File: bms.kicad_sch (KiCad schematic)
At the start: 0 parts

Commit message: Ajout du BMS
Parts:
- added C10, C13, C14, C15, C21, C8, C9: 100nF, Capacitor_SMD:C_0805_2012Metric, symbol local:C_0402
- added C11, C23, C24, C25: 1µF, Capacitor_SMD:C_0805_2012Metric, symbol local:C_0402
- added C12: 47nF, Capacitor_SMD:C_0805_2012Metric, symbol local:C_0402
- added C16: 20µF, Capacitor_SMD:C_0805_2012Metric, symbol local:C_0402
- added C17: 2.2µF, Capacitor_SMD:C_0805_2012Metric, symbol local:C_0402
- added C18, C19, C20: 220nF, Capacitor_SMD:C_0805_2012Metric, symbol local:C_0402
- added C22: 100pF, Capacitor_SMD:C_0805_2012Metric, symbol local:C_0402
- added C6: 42nF, Capacitor_SMD:C_0805_2012Metric, symbol local:C_0402
- added C7: 1nF, Capacitor_SMD:C_0805_2012Metric, symbol local:C_0402
- added IC3: BQ24810RUYR, local:QFN40P400X400X80-29N-D, symbol local:BQ24810RUYR
- added J2: S4B-XH-A-1, S4B-XH-A-1:JST_S4B-XH-A-1, symbol local:S4B-XH-A-1
- added L2: 3.3µH, symbol Device:L
- added R10, R17, R9: 4k, Resistor_SMD:R_0805_2012Metric, symbol local:R
- added R11: 866k, Resistor_SMD:R_0805_2012Metric, symbol local:R
- added R12: 133k, Resistor_SMD:R_0805_2012Metric, symbol local:R
- added R13: 0.01, Resistor_SMD:R_0805_2012Metric, symbol local:R
- added R14, R15, R16, R18, R19, R20, R22, R23: 10, Resistor_SMD:R_0805_2012Metric, symbol local:R
- added R21, R6: 0.001, Resistor_SMD:R_0805_2012Metric, symbol local:R
- added R24, R25: 5.1k, Resistor_SMD:R_0805_2012Metric, symbol local:R
- added R7, R8: 4.99, Resistor_SMD:R_0805_2012Metric, symbol local:R
- added U1, U2, U3, U4, U5, U7, U8: XSM6K519NW, local:DFN2020MD-6_SOT1220_NEX, symbol local:XSM6K519NW
- added U6: BQ76905RGRR, local:IC_BQ76905RGRR, symbol local:BQ76905RGRR
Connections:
- new net: C12.1, IC3.27 (PHASE), L2.1, U3.4, U3.7, U4.1, U4.2, U4.5, U4.6, U4.8
- new net: IC3.23 (LODRV), U4.3
- new net: C10.2, C8.2, IC3.1 (ACN), R8.2
- new net: IC3.17 (BATSRC), R16.1
- new net: IC3.18 (BATDRV), R17.1
- new net: IC3.19 (SRN), R14.1
- new net: C8.1, C9.2, IC3.2 (ACP), R7.2
- new net: IC3.20 (SRP), R15.1
- new net: C17.2, IC3.24 (REGN)
- new net: C12.2, IC3.25 (BTST)
- new net: IC3.26 (HIDRV), U3.3
- new net: IC3.3 (CMSRC), R10.2
- new net: IC3.4 (ACDRV), R9.2
- new net: IC3.6 (ACDET), R11.2, R12.1
- new net: C18.1, C19.2, R19.1, U6.1 (VC3A), U6.19 (VC4A), U6.2 (VC3B), U6.20 (VC4B), U6.3 (VC2)
- new net: C13.1, C14.2, L2.2, R13.1, R16.2, U5.4, U5.7
- new net: C6.1, R10.1, U1.4, U1.7, U2.4, U2.7
- new net: C21.2, C22.2, R22.1, U6.10 (CHG)
- new net: R21.1, R22.2, U8.4, U8.7
- new net: C6.2, C7.2, R9.1, U1.3, U2.3
- new net: R6.2, R7.1, U2.1, U2.2, U2.5, U2.6, U2.8
- new net: C20.1, R20.1, U6.4 (VC1)
- new net: J2.2, R20.2
- new net: U7.1, U7.2, U7.5, U7.6, U7.8, U8.1, U8.2, U8.5, U8.6, U8.8
- new net: R25.2, U7.3
- new net: J2.3, R19.2
- new net: J2.4, R18.2
- new net: C21.1, C22.1, R23.1, U6.9 (DSG)
- new net: C19.1, R18.1, U6.18 (VC5)
- new net: C15.1, R14.2
- new net: R24.1, U6.6 (SRP)
- new net: R24.2, U8.3
- new net: R25.1, U6.7 (SRN)
- new net: C14.1, R15.2
- new net: R17.2, U5.3
- new net +BATT: C23.2, U6.17 (BAT)
- new net -BATT: U7.4, U7.7
- new net GND: C10.1, C11.1, C16.1, C17.1, C18.2, C20.2, C23.1, C24.1, C25.1, C9.1, IC3.22 (GND), IC3.29 (EP), J2.1, R12.2, R21.2, R23.2, U4.4, U4.7, U6.11 (VSS), U6.21 (EXP), U6.5 (VC0)
- new net REGOUT: C24.2, U6.15 (REGOUT)
- new net REGSRC: C25.2, U6.16 (REGSRC)
- new net SCL: IC3.12 (SCL), U6.13 (SDA)
- new net SDA: IC3.11 (SDA), U6.12 (SCL)
- new net V_BATT: C13.2, C15.2, C16.2, R13.2
- new net V_BMS_IN: C11.2, C7.1, IC3.28 (VCC), R11.1, U1.1, U1.2, U1.5, U1.6, U1.8
- new net V_BMS_OUT: R6.1, R8.1, U3.1, U3.2, U3.5, U3.6, U3.8, U5.1, U5.2, U5.5, U5.6, U5.8
- new net ~{ALERT}: U6.14 (ALERT)
- no-connect marks 0 -> 9
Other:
- note added: "Battery monitoring"
- note added: "Battery power management"
- note added: "Near VCC IC3"
- note added: "charge Li-ion 3S"

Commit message: Update BMS
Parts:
- added C26: 2.2µF, Capacitor_SMD:C_0805_2012Metric, symbol local:C_0402
- added C27, C28: 100pF, Capacitor_SMD:C_0805_2012Metric, symbol local:C_0402
- added C29: 100µF, Capacitor_SMD:C_0805_2012Metric, symbol local:C_0402
- added C30: 100nF, Capacitor_SMD:C_0805_2012Metric, symbol local:C_0402
- added D1, D2: ~, local:DIO_MM3Z3V0T1G, symbol Device:D_Zener
- added IC4: LM2931AD33R, local:SOIC127P600X175-8N, symbol local:LM2931AD33R
- added R26, R27, R28: 200, Resistor_SMD:R_0805_2012Metric, symbol local:R
- added R29: 30.1k, Resistor_SMD:R_0805_2012Metric, symbol local:R
- added R30, R32: 68.1k, Resistor_SMD:R_0805_2012Metric, symbol local:R
- added R31, R33: 100k, Resistor_SMD:R_0805_2012Metric, symbol local:R
- added TP1: BATT+, symbol Connector:TestPoint
- added TP2: BATT-, symbol Connector:TestPoint
- added TP3: VC3, symbol Connector:TestPoint
- added TP4: VC2, symbol Connector:TestPoint
- added TP5: VC1, symbol Connector:TestPoint
- added TP6: V_SYS, symbol Connector:TestPoint
- R10, R9: value 4k -> 4.02k
- R11: value 866k -> 430k
- R12: value 133k -> 66.5k
- R6: value 0.001 -> 0.01
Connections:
- net +BATT: now also TP1.1
- net -BATT: now also TP2.1
- net GND: now also C26.1, C27.1, C28.1, C29.1, C30.1, IC4.2 (GND[4]), IC4.3 (GND[4]), IC4.5 (INHIBIT), IC4.6 (GND[4]), IC4.7 (GND[4]), R28.1, R29.1, R31.2, R33.2
- net V_BATT: now also R32.1
- net V_BMS_IN: now also C26.2, D1.2 (A); no longer C11.2, IC3.28 (VCC)
- net V_BMS_OUT: now also D2.2 (A), TP6.1
- net ~{ALERT}: now also IC3.10 (~{PROCHOT})
- net CMPIN: now reaches IC3.13 (CMPIN)
- net CMPIN: now also R32.2, R33.1
- net ~{BATPRES}: now reaches IC3.14 (CMPOUT)
- net ~{BATPRES}: now also IC3.15 (~{BATPRES})
- net ILIM: now reaches IC3.21 (ILIM)
- net ILIM: now also R30.2, R31.1
- net CHARGING: now reaches IC3.5 (ACOK)
- net at IC3.7 (IADP): now also C27.2
- net at IC3.8 (IDCHG): now also C28.2
- net at IC3.9 (PMON): now also R29.2
- net VC1: now reaches J2.2, R20.2
- net VC1: now also R27.1, R28.2, TP5.1
- net VC2: now reaches J2.3, R19.2
- net VC2: now also R26.1, R27.2, TP4.1
- net VC3: now reaches J2.4, R18.2
- net VC3: now also R26.2, TP3.1
- new net: C29.2, IC4.1 (VOUT), R30.1
- new net: C30.2, IC4.8 (VIN)
- new net VCC: C11.2, D1.1 (K), D2.1 (K), IC3.28 (VCC)
- no-connect marks 9 -> 2
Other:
- note added: "Le onnecteur batterie est relié par deux cable soudés sur ces 2 pads"
- note added: "Le test avec une alim implique ce jeu de résistance"
- note removed: "Near VCC IC3"
- note removed: "charge Li-ion 3S"
- moved on the sheet: C11, C17, C18, C19, C20, C23, C24, C25, J2, R11, R12, R18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

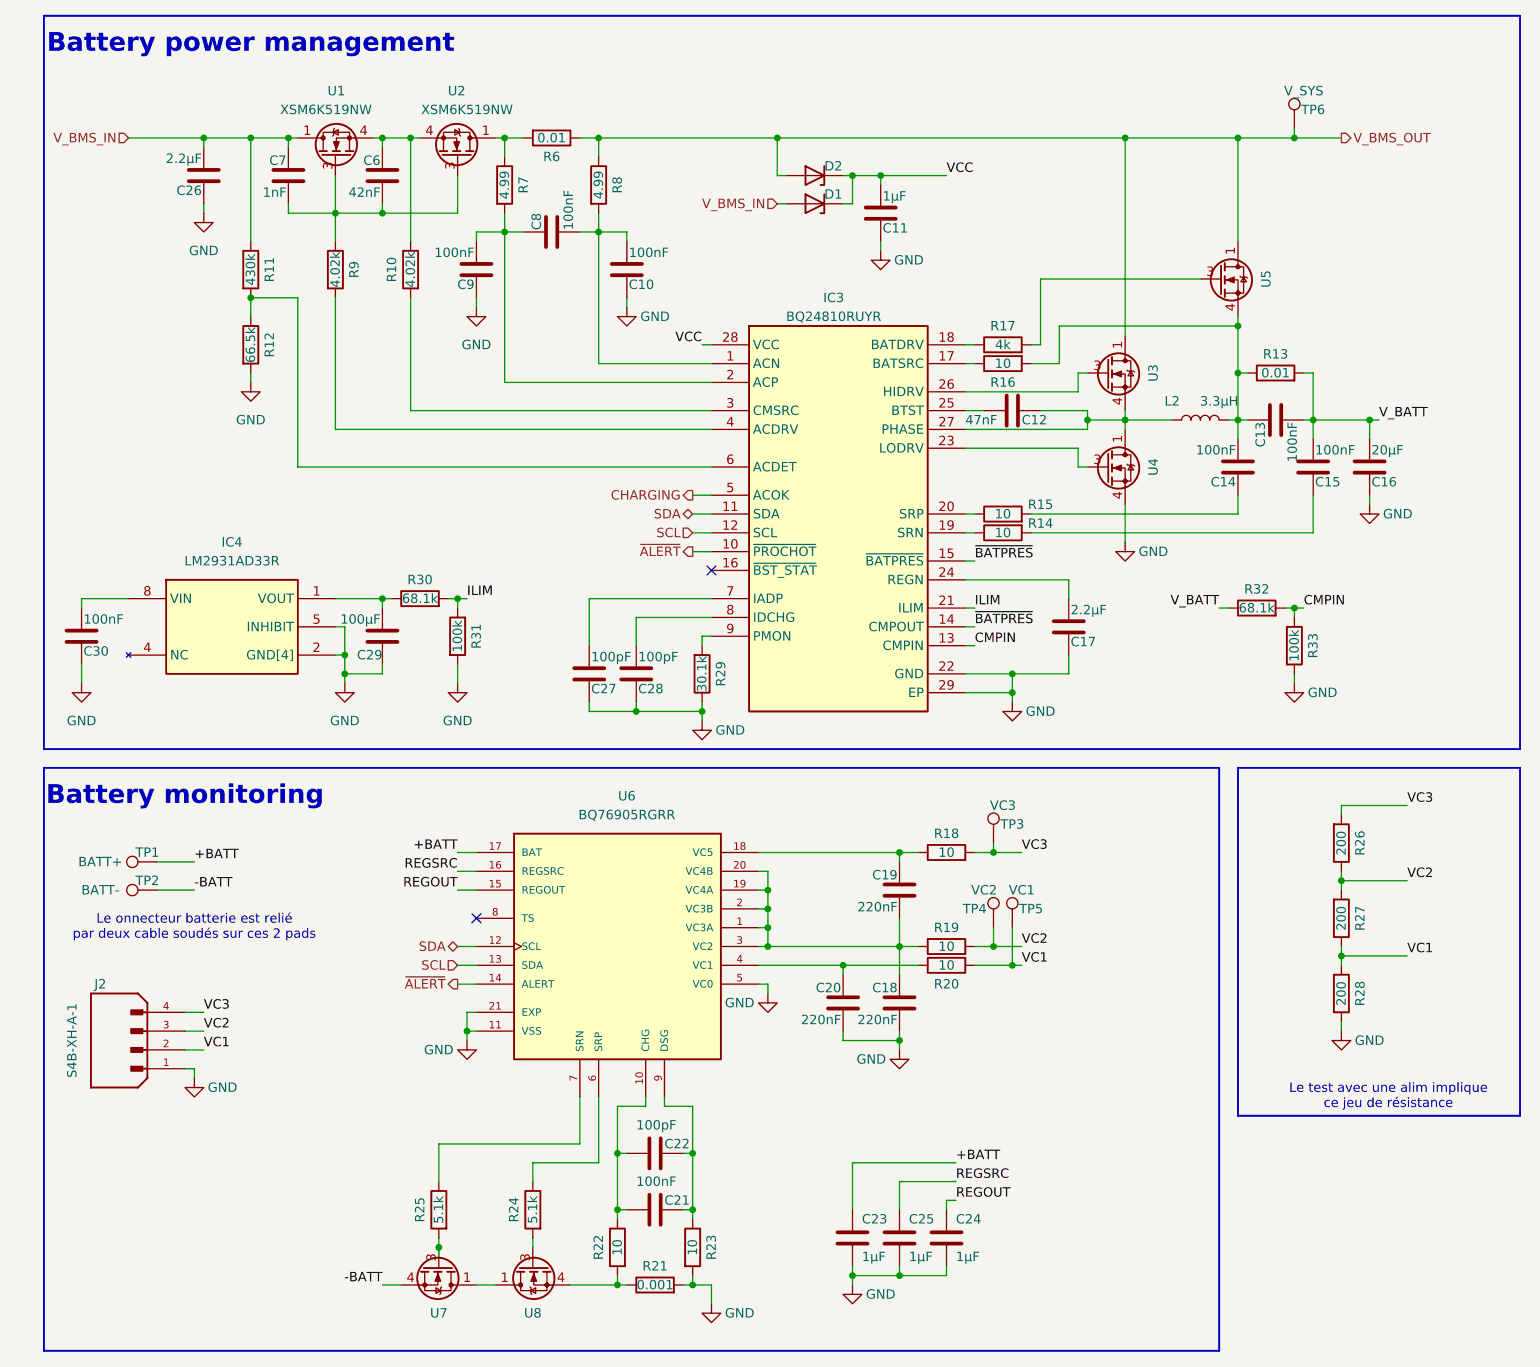
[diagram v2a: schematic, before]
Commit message: Version 0. Schémas finalisés. Mise à jour des résistances en série E12. Réduction de la BOM.
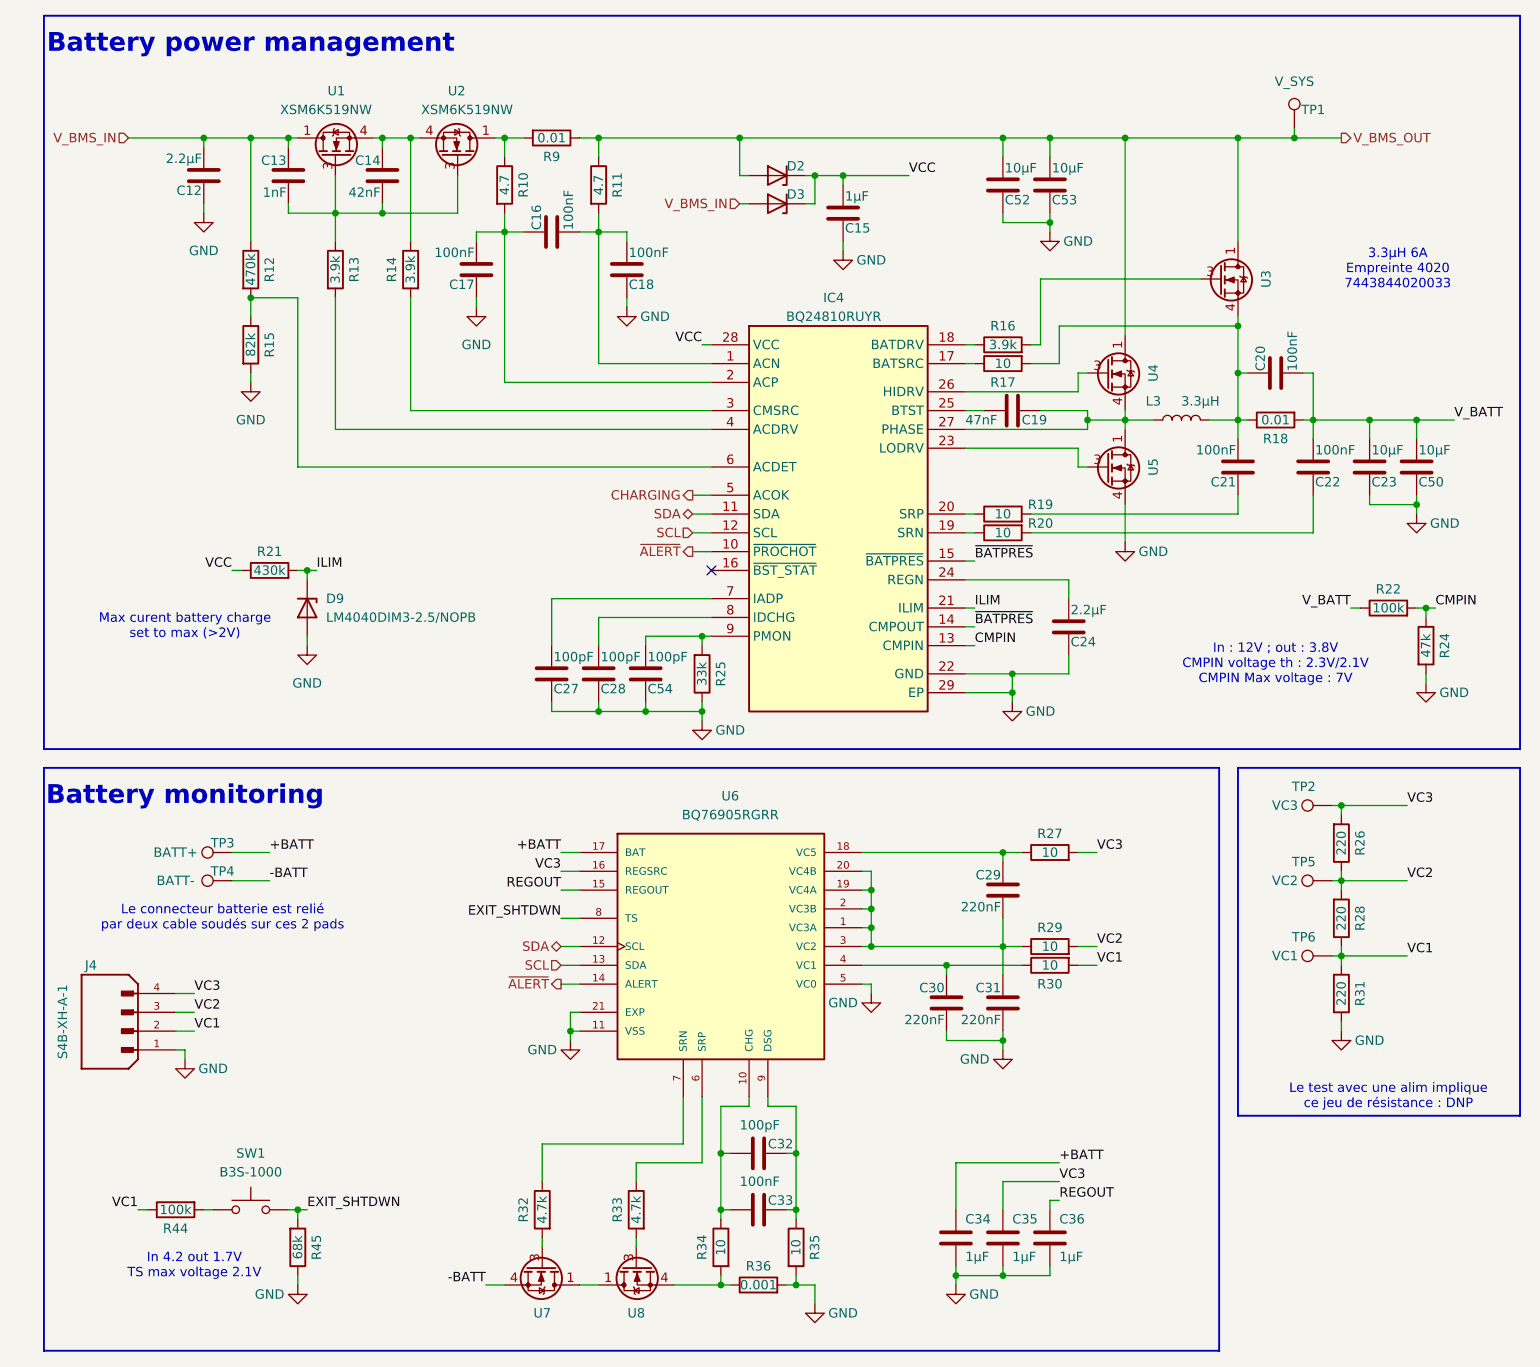
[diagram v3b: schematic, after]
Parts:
- removed C29: 100µF, Capacitor_SMD:C_0805_2012Metric, symbol local:C_0402
- removed C30: 100nF, Capacitor_SMD:C_0805_2012Metric, symbol local:C_0402
- removed IC4: LM2931AD33R, local:SOIC127P600X175-8N, symbol local:LM2931AD33R
- removed R30: 68.1k, Resistor_SMD:R_0805_2012Metric, symbol local:R
- removed R31: 100k, Resistor_SMD:R_0805_2012Metric, symbol local:R
- added C50, C52, C53: 10µF, Capacitor_SMD:C_0805_2012Metric, symbol local:C_0402
- added C54: 100pF, Capacitor_SMD:C_0805_2012Metric, symbol local:C_0402
- added D9: LM4040DIM3-2.5/NOPB, local:SOT95P237X112-3N, symbol Device:D_Zener
- added R21: 430k, Resistor_SMD:R_0805_2012Metric, symbol local:R
- added R44: 100k, Resistor_SMD:R_0805_2012Metric, symbol local:R
- added R45: 68k, Resistor_SMD:R_0805_2012Metric, symbol local:R
- added SW1: B3S-1000, local:SW_SPST_B3S-1000, symbol Switch:SW_Push
- C23: renamed from C16; value 20µF -> 10µF
- L3: renamed from L2; footprint (none) -> local:L_Wuerth_MAPI-4020
- R10: renamed from R7; value 4.99 -> 4.7
- R11: renamed from R8; value 4.99 -> 4.7
- R12: renamed from R11; value 430k -> 470k
- R13: renamed from R9; value 4.02k -> 3.9k
- R14: renamed from R10; value 4.02k -> 3.9k
- R15: renamed from R12; value 66.5k -> 82k
- R16: renamed from R17; value 4k -> 3.9k
- R22: renamed from R32; value 68.1k -> 100k
- R24: renamed from R33; value 100k -> 47k
- R25: renamed from R29; value 30.1k -> 33k
- R26: value 200 -> 220
- R28: renamed from R27; value 200 -> 220
- R31: renamed from R28; value 200 -> 220
- R32: renamed from R25; value 5.1k -> 4.7k
- R33: renamed from R24; value 5.1k -> 4.7k
- renumbered C26 to C12, C7 to C13, C6 to C14, C11 to C15, C8 to C16, C9 to C17, C10 to C18, C12 to C19, C13 to C20, C14 to C21, C15 to C22, C17 to C24, C19 to C29, C20 to C30, C18 to C31, C22 to C32, C21 to C33, C23 to C34, C25 to C35, C24 to C36, D1 to D3, IC3 to IC4, J2 to J4, R16 to R17, R13 to R18, R15 to R19, R14 to R20, R18 to R27, R19 to R29, R20 to R30, R22 to R34, R23 to R35, R21 to R36, R6 to R9, TP6 to TP1, TP3 to TP2, TP1 to TP3, TP2 to TP4, TP4 to TP5, TP5 to TP6, U5 to U3, U3 to U4, U4 to U5
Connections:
- net REGSRC is gone; now on net VC3: C35.2, U6.16 (REGSRC)
- net GND: now also C50.1, C52.1, C53.1, C54.1, D9.2 (A), R45.1
- net ILIM: now also D9.1 (K), R21.2
- net VC1: now also R44.1
- net VCC: now also R21.1
- net V_BATT: now also C50.2
- net V_BMS_OUT: now also C52.2, C53.2
- net at IC4.9 (PMON), R25.2: now also C54.2
- net EXIT_SHTDWN: now reaches U6.8 (TS)
- net EXIT_SHTDWN: now also R45.2, SW1.2
- new net: R44.2, SW1.1
- no-connect marks 2 -> 1
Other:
- note added: "3.3µH 6A Empreinte 4020 7443844020033"
- note added: "In 4.2 out 1.7V TS max voltage 2.1V"
- note added: "In : 12V ; out : 3.8V CMPIN voltage th : 2.3V/2.1V CMPIN Max voltage : 7V"
- note added: "Le connecteur batterie est relié par deux cable soudés sur ces 2 pads"
- note added: "Le test avec une alim implique ce jeu de résistance : DNP"
- note added: "Max curent battery charge set to max (>2V)"
- note removed: "Le onnecteur batterie est relié par deux cable soudés sur ces 2 pads"
- note removed: "Le test avec une alim implique ce jeu de résistance"
- moved on the sheet: C15, C20, C27, C28, C29, C30, C31, C32, C33, C34, C35, C36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
